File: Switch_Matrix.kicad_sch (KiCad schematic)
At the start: 147 parts, among them SW1 SW_Push_45deg, SW10 SW_Push_45deg, SW11 SW_Push_45deg, SW12 SW_Push_45deg, SW12(2)1 SW_Push_45deg, SW13 SW_Push_45deg, SW14 SW_Push_45deg, SW15 SW_Push_45deg, SW16 SW_Push_45deg, SW17 SW_Push_45deg, SW18 SW_Push_45deg, SW19 SW_Push_45deg, SW2 SW_Push_45deg, SW20 SW_Push_45deg, SW21 SW_Push_45deg, SW22 SW_Push_45deg, SW23 SW_Push_45deg, SW24 SW_Push_45deg, SW24(1.5)1 SW_Push_45deg, SW25 SW_Push_45deg, SW25(1.5)1 SW_Push_45deg, SW26 SW_Push_45deg, SW26(2)1 SW_Push_45deg, SW26(ISO)1 SW_Push_45deg, SW27(1.25)1 SW_Push_45deg, SW27(1.5)1 SW_Push_45deg, SW27(ortho)1 SW_Push_45deg, SW28 SW_Push_45deg, SW28(1.5stagger)1 SW_Push_45deg, SW28(ortho)1 SW_Push_45deg, SW29 SW_Push_45deg, SW29(1.5stagger)1 SW_Push_45deg, SW29(ortho)1 SW_Push_45deg, SW3 SW_Push_45deg, SW30 SW_Push_45deg, SW30(1.5stagger)1 SW_Push_45deg, SW30(ortho)1 SW_Push_45deg, SW31 SW_Push_45deg, SW31(1.5stagger)1 SW_Push_45deg, SW31(ortho)1 SW_Push_45deg, SW32 SW_Push_45deg, SW32(1.5stagger)1 SW_Push_45deg, SW32(ortho)1 SW_Push_45deg, SW33 SW_Push_45deg, SW33(1.5stagger)1 SW_Push_45deg, SW33(ortho)1 SW_Push_45deg, SW34 SW_Push_45deg, SW34(1.5stagger)1 SW_Push_45deg, SW34(ortho)1 SW_Push_45deg, SW35 SW_Push_45deg, SW35(1.5stagger)1 SW_Push_45deg, SW35(ortho)1 SW_Push_45deg, SW36 SW_Push_45deg, SW36(1.5stagger)1 SW_Push_45deg, SW36(ortho)1 SW_Push_45deg, SW37 SW_Push_45deg, SW37(1.5stagger)1 SW_Push_45deg, SW37(ortho)1 SW_Push_45deg, SW38(1.25)1 SW_Push_45deg, SW38(1.5)1 SW_Push_45deg, SW38(ortho)1 SW_Push_45deg, SW39 SW_Push_45deg, SW39(1.5)1 SW_Push_45deg, SW4 SW_Push_45deg, SW40 SW_Push_45deg, SW40(3)1 SW_Push_45deg, SW41 SW_Push_45deg, SW41(1.5)1 SW_Push_45deg, SW42(1.25)1 SW_Push_45deg, SW42(1.5)1 SW_Push_45deg, SW42(3)1 SW_Push_45deg, SW43(1.75)1 SW_Push_45deg, SW43(2)1 SW_Push_45deg, SW44(3)1 SW_Push_45deg, SW44(4)1 SW_Push_45deg, SW44(6)1 SW_Push_45deg, SW45(1.75)1 SW_Push_45deg, SW45(2)1 SW_Push_45deg, SW46(1.25)1 SW_Push_45deg, SW46(1.5)1 SW_Push_45deg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

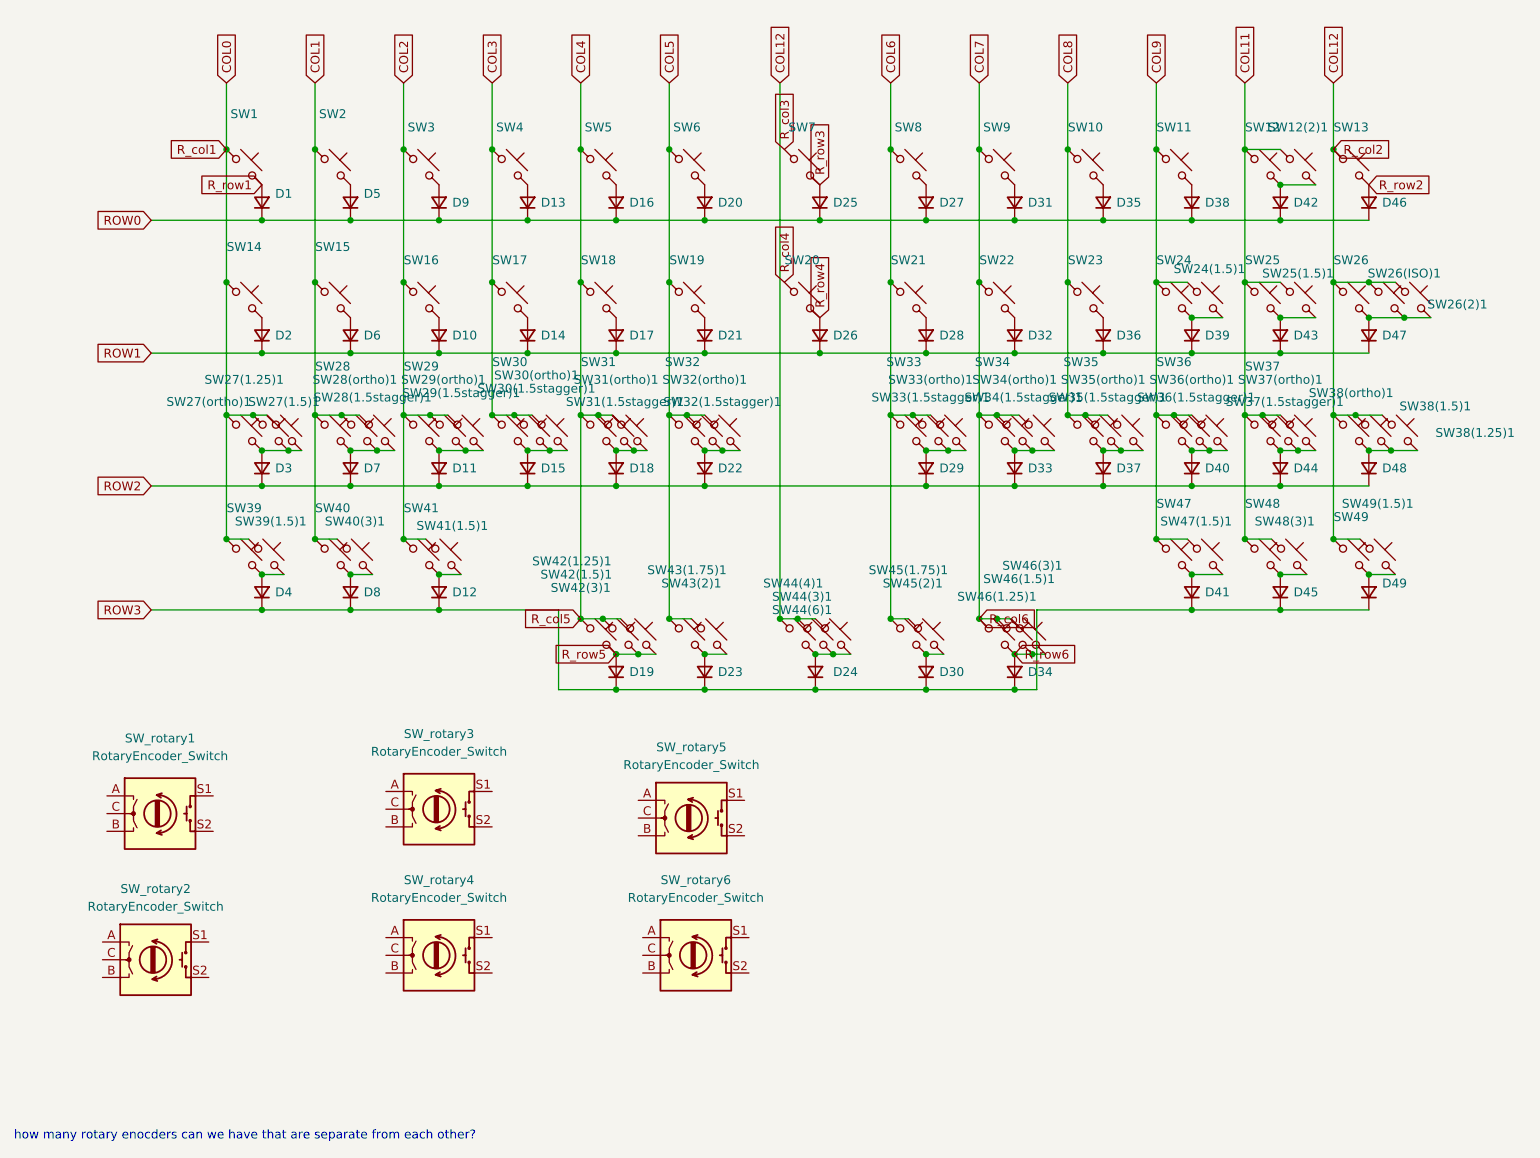
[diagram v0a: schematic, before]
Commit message: rp2040 pcb file and schematic created
MCU & USB component placement

early matrix routing
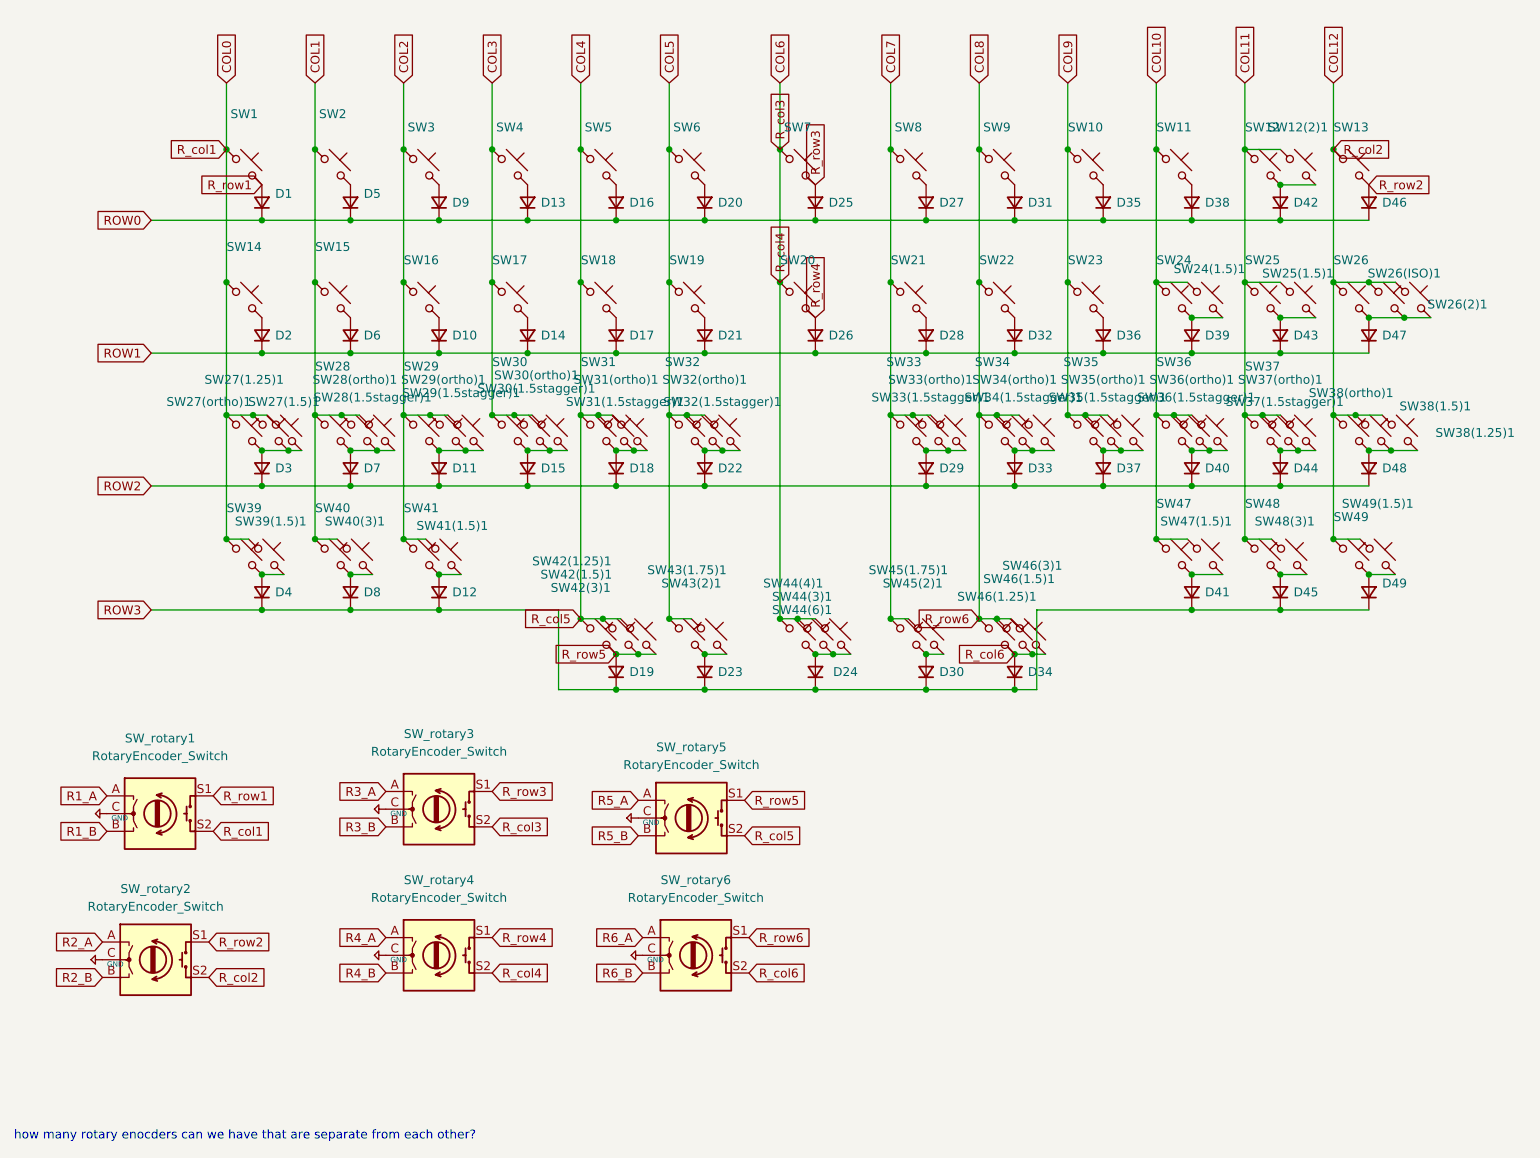
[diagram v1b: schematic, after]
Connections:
- net R_col3 is gone; now on net COL6: SW7.1
- net R_col4 is gone; now on net COL6: SW20.1
- net R_row6 is gone; now on net R_col6: D34.2 (A), SW46(1.25)1.2, SW46(1.5)1.2, SW46(3)1.2
- net COL0: now also SW_rotary1.S2
- net COL12: now also SW_rotary2.S2; no longer SW44(3)1.1, SW44(4)1.1, SW44(6)1.1
- net COL4: now also SW_rotary5.S2
- net COL6: now also SW44(3)1.1, SW44(4)1.1, SW44(6)1.1, SW_rotary3.S2, SW_rotary4.S2; no longer SW21.1, SW33(1.5stagger)1.1, SW33(ortho)1.1, SW33.1, SW45(1.75)1.1, SW45(2)1.1, SW8.1
- net COL7: now also SW21.1, SW33(1.5stagger)1.1, SW33(ortho)1.1, SW33.1, SW45(1.75)1.1, SW45(2)1.1, SW8.1; no longer SW22.1, SW34(1.5stagger)1.1, SW34(ortho)1.1, SW34.1, SW46(1.25)1.1, SW46(1.5)1.1, SW46(3)1.1, SW9.1
- net COL8: now also SW22.1, SW34(1.5stagger)1.1, SW34(ortho)1.1, SW34.1, SW46(1.25)1.1, SW46(1.5)1.1, SW46(3)1.1, SW9.1, SW_rotary6.S1; no longer SW10.1, SW23.1, SW35(1.5stagger)1.1, SW35(ortho)1.1, SW35.1
- net COL9: now also SW10.1, SW23.1, SW35(1.5stagger)1.1, SW35(ortho)1.1, SW35.1; no longer SW11.1, SW24(1.5)1.1, SW24.1, SW36(1.5stagger)1.1, SW36(ortho)1.1, SW36.1, SW47(1.5)1.1, SW47.1
- net R_row1: now also SW_rotary1.S1
- net R_row2: now also SW_rotary2.S1
- net R_row3: now also SW_rotary3.S1
- net R_row4: now also SW_rotary4.S1
- net R_row5: now also SW_rotary5.S1
- net R3_A: now reaches SW_rotary3.A
- net R3_B: now reaches SW_rotary3.B
- net +5V: now reaches SW_rotary3.C
- net +5V: now also SW_rotary1.C, SW_rotary2.C, SW_rotary4.C, SW_rotary5.C, SW_rotary6.C
- net R1_A: now reaches SW_rotary1.A
- net R1_B: now reaches SW_rotary1.B
- net R2_A: now reaches SW_rotary2.A
- net R2_B: now reaches SW_rotary2.B
- net R4_A: now reaches SW_rotary4.A
- net R4_B: now reaches SW_rotary4.B
- net R6_A: now reaches SW_rotary6.A
- net R6_B: now reaches SW_rotary6.B
- net R_col6: now reaches SW_rotary6.S2
- net R5_A: now reaches SW_rotary5.A
- net R5_B: now reaches SW_rotary5.B
- new net COL10: SW11.1, SW24(1.5)1.1, SW24.1, SW36(1.5stagger)1.1, SW36(ortho)1.1, SW36.1, SW47(1.5)1.1, SW47.1
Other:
- moved on the sheet: D25, D26, SW20, SW7

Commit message: MCU routing, RGB leds
MCU first routing draft finished

added RGB leds instead of diodes
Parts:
- SW44(4)1: footprint (none) -> CherryMX_4.00u:CherryMX_4.00u
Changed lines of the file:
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@@
       (effects (font (size 1.27 1.27)) hide)
     )
-    (property "Footprint" "" (id 2) (at 137.795 120.015 0)
+    (property "Footprint" "CherryMX_4.00u:CherryMX_4.00u" (id 2) (at 137.795 120.015 0)
       (effects (font (size 1.27 1.27)) hide)
     )

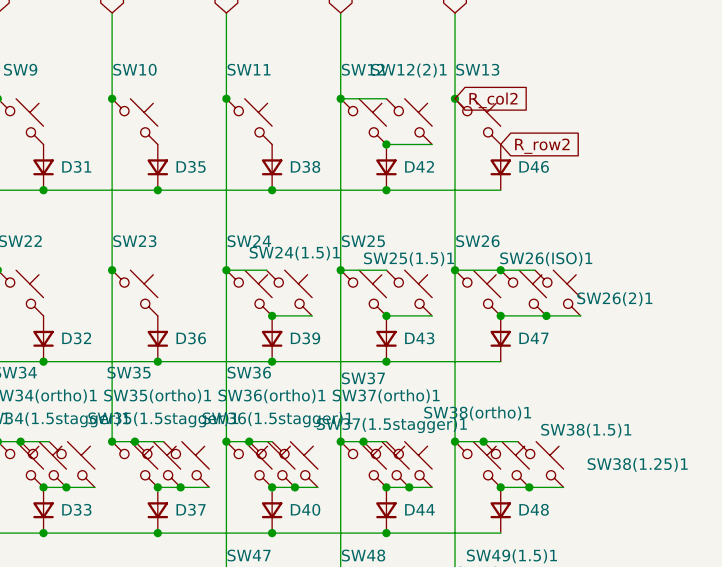
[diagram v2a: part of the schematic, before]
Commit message: changed MCU placement, redid routing
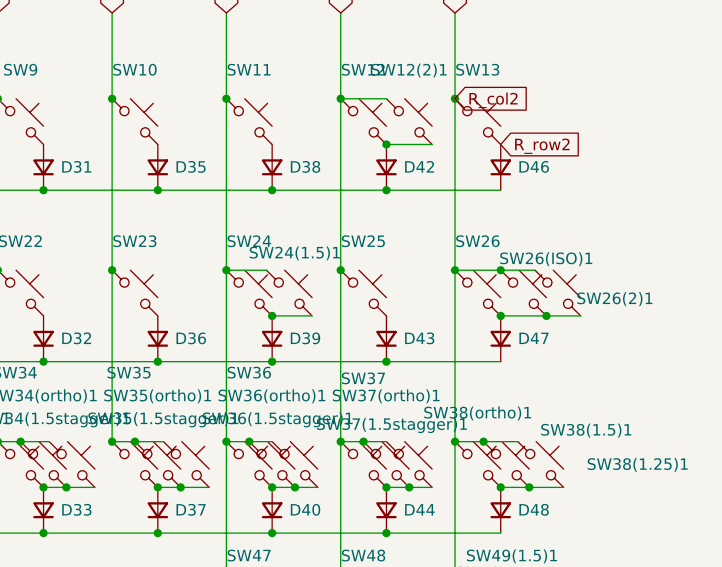
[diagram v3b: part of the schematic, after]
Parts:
- removed SW25(1.5)1: SW_Push_45deg, MX_Only:MXOnly-1.5U-NoLED, symbol Switch:SW_Push_45deg
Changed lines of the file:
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@@
   (junction (at 154.305 88.265) (diameter 0) (color 0 0 0 0)
   )
-  (junction (at 207.01 74.295) (diameter 0) (color 0 0 0 0)
-  )
   (junction (at 60.96 98.425) (diameter 0) (color 0 0 0 0)
   )
@@
     (stroke (width 0) (type default) (color 0 0 0 0))
   )
-  (wire (pts (xy 212.09 74.295) (xy 207.01 74.295))
-    (stroke (width 0) (type default) (color 0 0 0 0))
-  )
   (wire (pts (xy 119.38 50.165) (xy 119.38 69.215))
     (stroke (width 0) (type default) (color 0 0 0 0))
@@
     (stroke (width 0) (type default) (color 0 0 0 0))
   )
-  (wire (pts (xy 207.01 69.215) (xy 201.93 69.215))
-    (stroke (width 0) (type default) (color 0 0 0 0))
-  )
   (wire (pts (xy 60.96 98.425) (xy 45.085 98.425))
     (stroke (width 0) (type default) (color 0 0 0 0))
@@
       (effects (font (size 1.27 1.27)) hide)
     )
-    (pin "1")
-    (pin "2")
-  )
-  (symbol (lib_id "Switch:SW_Push_45deg") (at 209.55 71.755 0) (unit 1)
-    (in_bom yes) (on_board yes)
-    (property "Reference" "SW25(1.5)1" (id 0) (at 209.55 67.945 0))
-    (property "Value" "SW_Push_45deg" (id 1) (at 209.55 66.675 0)
-      (effects (font (size 1.27 1.27)) hide)
-    )
-    (property "Footprint" "MX_Only:MXOnly-1.5U-NoLED" (id 2) (at 209.55 71.755 0)
-      (effects (font (size 1.27 1.27)) hide)
-    )
-    (property "Datasheet" "~" (id 3) (at 209.55 71.755 0)
-      (effects (font (size 1.27 1.27)) hide)
-    )

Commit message: galvy edits - start routing testing
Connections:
- net R3_A renamed PD5
- net R3_B renamed PD2
- net R4_A renamed SDA
- net R4_B renamed SCL
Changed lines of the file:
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@@
+    )
+  )
+  (global_label "SDA" (shape input) (at 78.74 163.195 180) (fields_autoplaced)
+    (effects (font (size 1.27 1.27)) (justify right))
+    (property "Intersheet References" "${INTERSHEET_REFS}" (id 0) (at 72.7588 163.1156 0)
+      (effects (font (size 1.27 1.27)) (justify right) hide)
     )
   )
@@
     )
   )
-  (global_label "R3_B" (shape input) (at 78.74 147.32 180) (fields_autoplaced)
-    (effects (font (size 1.27 1.27)) (justify right))
-    (property "Intersheet References" "${INTERSHEET_REFS}" (id 0) (at 71.6098 147.2406 0)
+  (global_label "PD2" (shape input) (at 78.74 147.32 180) (fields_autoplaced)
+    (effects (font (size 1.27 1.27)) (justify right))
+    (property "Intersheet References" "${INTERSHEET_REFS}" (id 0) (at 72.6663 147.3994 0)
       (effects (font (size 1.27 1.27)) (justify right) hide)
     )
@@
     )
   )
-  (global_label "R3_A" (shape input) (at 78.74 142.24 180) (fields_autoplaced)
-    (effects (font (size 1.27 1.27)) (justify right))
-    (property "Intersheet References" "${INTERSHEET_REFS}" (id 0) (at 71.7912 142.1606 0)
-      (effects (font (size 1.27 1.27)) (justify right) hide)
-    )
-  )
   (global_label "COL6" (shape input) (at 135.255 40.64 90) (fields_autoplaced)
     (effects (font (size 1.27 1.27)) (justify left))
@@
     )
   )
-  (global_label "R4_B" (shape input) (at 78.74 168.275 180) (fields_autoplaced)
-    (effects (font (size 1.27 1.27)) (justify right))
-    (property "Intersheet References" "${INTERSHEET_REFS}" (id 0) (at 71.6098 168.1956 0)
-      (effects (font (size 1.27 1.27)) (justify right) hide)
-    )
-  )
   (global_label "R_row6" (shape input) (at 163.83 117.475 180) (fields_autoplaced)
     (effects (font (size 1.27 1.27)) (justify right))
@@
     )
   )
-  (global_label "R4_A" (shape input) (at 78.74 163.195 180) (fields_autoplaced)
-    (effects (font (size 1.27 1.27)) (justify right))
-    (property "Intersheet References" "${INTERSHEET_REFS}" (id 0) (at 71.7912 163.1156 0)
-      (effects (font (size 1.27 1.27)) (justify right) hide)
-    )
-  )
   (global_label "ROW0" (shape input) (at 45.085 60.325 180) (fields_autoplaced)
     (effects (font (size 1.27 1.27)) (justify right))
@@
     )
   )
+  (global_label "PD5" (shape input) (at 78.74 142.24 180) (fields_autoplaced)
+    (effects (font (size 1.27 1.27)) (justify right))
+    (property "Intersheet References" "${INTERSHEET_REFS}" (id 0) (at 72.6663 142.3194 0)
+      (effects (font (size 1.27 1.27)) (justify right) hide)
+    )
+  )
   (global_label "R_row5" (shape input) (at 130.175 143.51 0) (fields_autoplaced)
     (effects (font (size 1.27 1.27)) (justify left))
@@
     )
   )
+  (global_label "SCL" (shape input) (at 78.74 168.275 180) (fields_autoplaced)
+    (effects (font (size 1.27 1.27)) (justify right))
+    (property "Intersheet References" "${INTERSHEET_REFS}" (id 0) (at 72.8193 168.1956 0)
+      (effects (font (size 1.27 1.27)) (justify right) hide)
+    )
+  )

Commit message: encoder, plate
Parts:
- SW_rotary1, SW_rotary2, SW_rotary3, SW_rotary4, SW_rotary5, SW_rotary6: footprint Keebio-Parts:RotaryEncoder_EC11-no-legs -> Keebio-Parts:RotaryEncoder_EC11_Nonplated
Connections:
- net +5V renamed GND

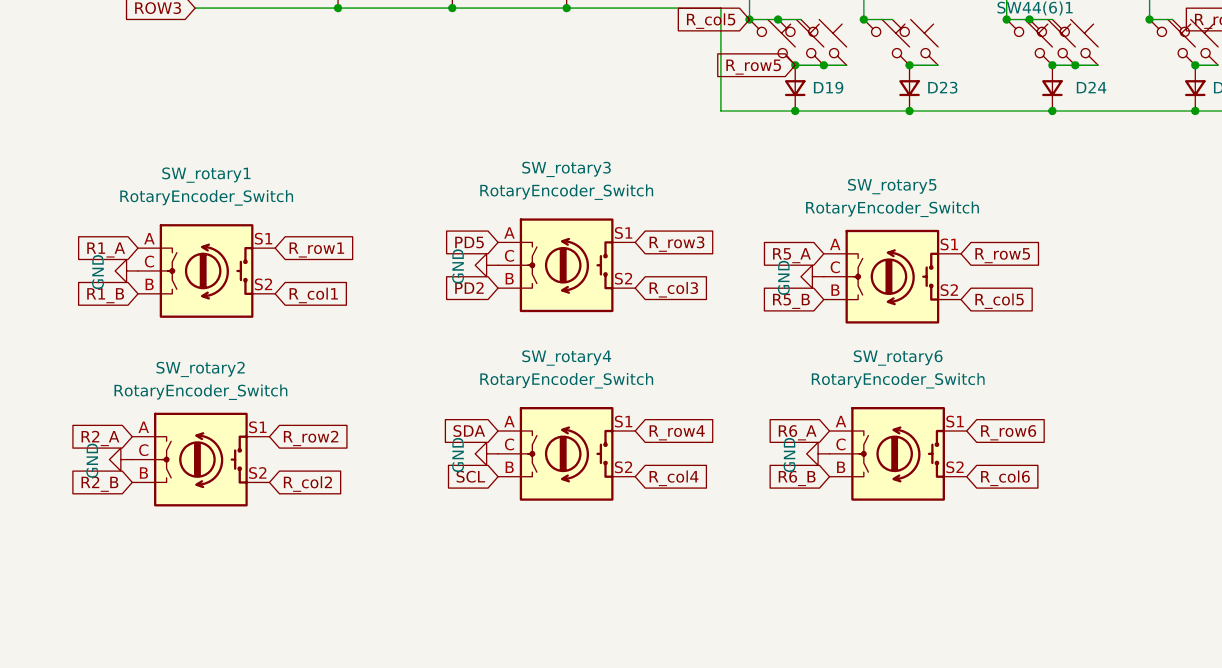
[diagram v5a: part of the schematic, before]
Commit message: first full routing
no error check, not very clean routing
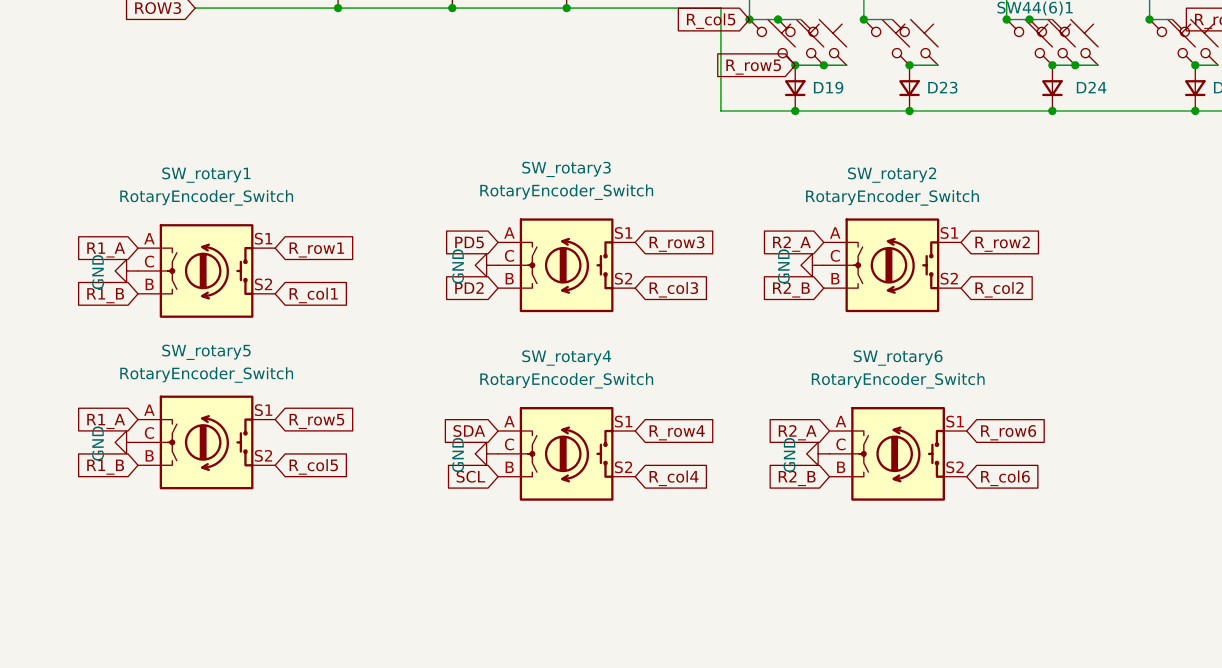
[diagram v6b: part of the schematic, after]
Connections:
- net R5_A is gone; now on net R1_A: SW_rotary5.A
- net R5_B is gone; now on net R1_B: SW_rotary5.B
- net R6_A is gone; now on net R2_A: SW_rotary6.A
- net R6_B is gone; now on net R2_B: SW_rotary6.B
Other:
- moved on the sheet: SW_rotary2, SW_rotary5
